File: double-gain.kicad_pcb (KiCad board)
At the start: 2 copper layers, 37.5 x 97.5 mm, 39 parts, among them J1 Conn_01x01_Female, J10 Conn_01x01_Female, J11 Conn_01x01_Female, J2 Conn_01x01_Female, J3 Conn_01x01_Female, J4 Conn_01x01_Female, J6 Conn_01x01_Female, J7 Conn_01x01_Female, J8 Conn_01x01_Female, J9 Conn_01x01_Female, U1 NE5534, U2 NE5534

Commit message: Add files via upload
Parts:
- renumbered C7 to C5, C8 to C7, C10 to C8

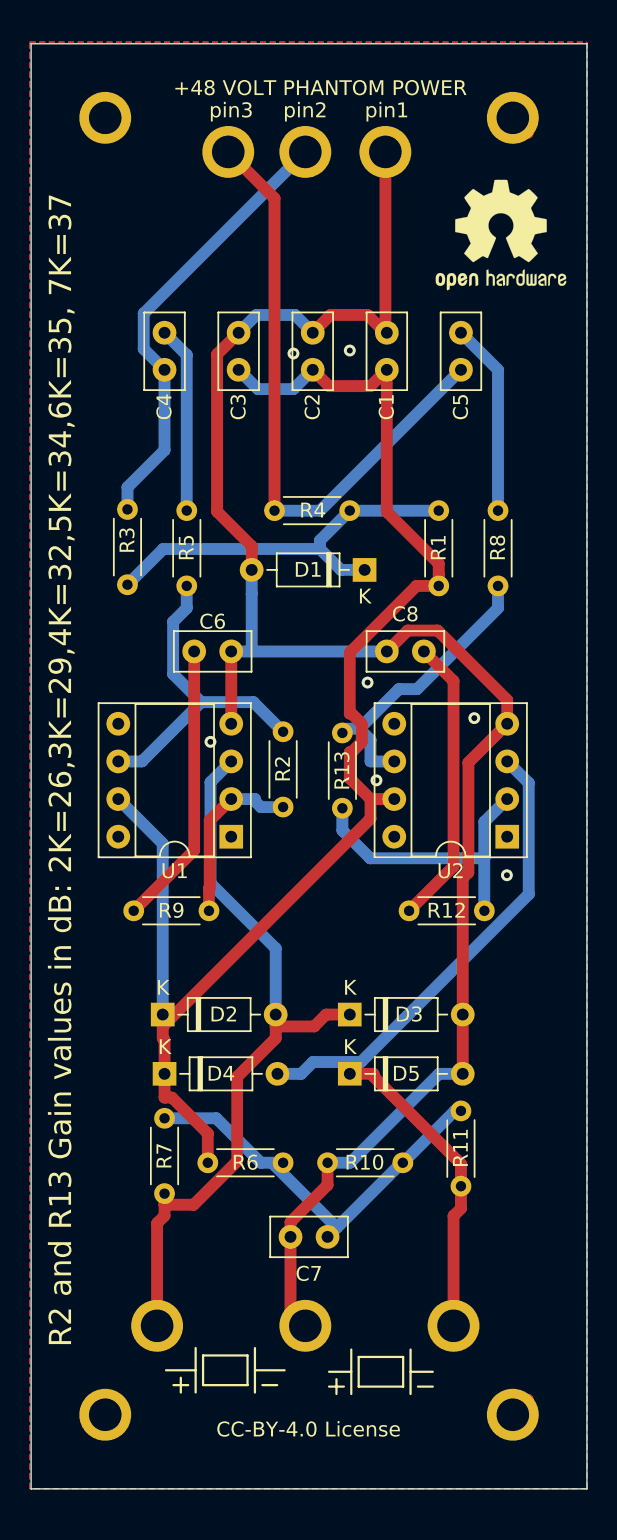
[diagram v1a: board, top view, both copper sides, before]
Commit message: Add files via upload
Replaced the opamp with a better one, with less power drain. Also added RF killer capacitor, C9 and C10.
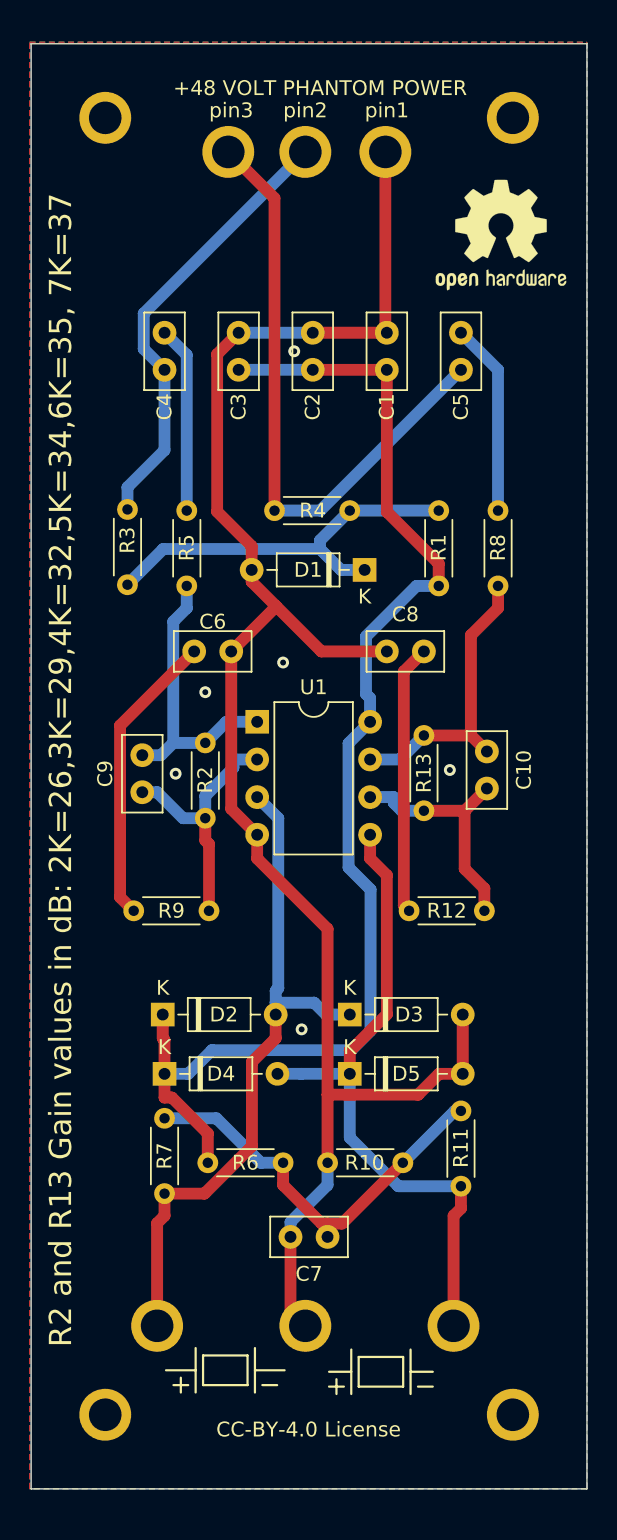
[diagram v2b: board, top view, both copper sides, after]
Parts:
- removed U2: NE5534, Package_DIP:DIP-8_W7.62mm_Socket
- added C10: 47uF, Capacitor_THT:C_Disc_D5.0mm_W2.5mm_P2.50mm, F.Cu at (68.2, 82.8)
- added C9: 47uF, Capacitor_THT:C_Disc_D5.0mm_W2.5mm_P2.50mm, F.Cu at (45.0, 83.0)
- D1: value 1N4746A (18V) -> HZ11B3-E
- U1: value NE5534 -> TL082; footprint Package_DIP:DIP-8_W7.62mm_Socket -> Package_DIP:DIP-8_W7.62mm
- moved U1 7.95 mm to (52.8, 78.2), turned to 0 degrees
- moved R13 5.50 mm to (64.0, 79.2)
- moved R2 5.30 mm to (49.2, 79.7)
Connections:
- R12 pad 2: Net-(R12-Pad2) -> Net-(C10-Pad1)
- R13 pad 1: Net-(R13-Pad1) -> Net-(C10-Pad2)
- R13 pad 2: Net-(R12-Pad2) -> Net-(C10-Pad1)
- R2 pad 1: Net-(R2-Pad1) -> Net-(C9-Pad2)
- R5 pad 2: Net-(R2-Pad1) -> Net-(C9-Pad2)
- R8 pad 2: Net-(R13-Pad1) -> Net-(C10-Pad2)
- U1 pad 1: Net-(U1-Pad1) -> Net-(C9-Pad2)
- U1 pad 5: Net-(U1-Pad5) -> ind
- U1 pad 6: Net-(R2-Pad1) -> Net-(C10-Pad1)
- U1 pad 7: VCC -> Net-(C10-Pad2)
- U1 pad 8: Net-(U1-Pad8) -> VCC
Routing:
- net Net-(R2-Pad1): track 22.6 -> 0.00 mm
- net Net-(R12-Pad2): track 20.0 -> 0.00 mm
- net Net-(C10-Pad2): track 0.00 -> 19.8 mm
- net Net-(C9-Pad2): track 0.00 -> 19.6 mm
- net Net-(R13-Pad1): track 19.6 -> 0.00 mm
- net Net-(C10-Pad1): track 0.00 -> 16.4 mm
- net VCC: track 97.2 -> 86.9 mm
- net ind: track 53.6 -> 45.4 mm
- net Net-(C9-Pad1): track 12.0 -> 17.7 mm
- net V-: track 123.8 -> 119.3 mm
- net Net-(D2-Pad2): track 51.0 -> 46.6 mm
- net Earth: track 3.04 -> 0.00 mm, vias 7 -> 6
- net Net-(C8-Pad2): track 19.6 -> 18.2 mm
- net Net-(C6-Pad2): track 19.2 -> 20.0 mm

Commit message: Add files via upload
fixed value of C9 and C10.
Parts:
- C10, C9: value 47uF -> 47pF
- U1: value TL082 -> TL082BCP

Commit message: Add files via upload
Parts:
- removed the C6 at (51.0, 73.5)
- removed the C8 at (61.5, 73.5)
- removed the J10 at (66.0, 119.0)
- removed J11: Conn_01x01_Female, MountingHole:MountingHole_2.2mm_M2_ISO7380_Pad
- removed REF**: OSHW-Logo2_9.8x8mm_SilkScreen, Symbol:OSHW-Logo2_9.8x8mm_SilkScreen
- added C10: 47uF, Capacitor_THT:CP_Radial_D8.0mm_P3.50mm, F.Cu at (68.5, 74.5)
- added C7: 47uF, Capacitor_THT:CP_Radial_D8.0mm_P3.50mm, F.Cu at (45.5, 74.5)
- added J5: Conn_01x01_Female, MountingHole:MountingHole_2.2mm_M2_ISO7380_Pad, F.Cu at (46.0, 118.8)
- added J6: Conn_01x01_Female, MountingHole:MountingHole_2.2mm_M2_ISO7380_Pad, F.Cu at (61.5, 40.0)
- moved J1 79.6 mm to (56.0, 40.0)
- moved J2 79.6 mm to (66.0, 118.8)
- moved J4 79.2 mm to (55.8, 118.8)
- moved J3 0.28 mm to (51.0, 40.0)
- moved C9 0.25 mm to (68.2, 83.0)
- moved R13 0.25 mm to (64.0, 79.4)
- moved U1 0.25 mm to (52.8, 78.0)
- renumbered C9 to C6, C7 to C8, C10 to C9, D4 to D2, D5 to D3, D2 to D4, D3 to D5, J9 to J10, J6 to J7, J7 to J8, J8 to J9, R2 to R11, R6 to R2, R11 to R3, R7 to R4, R3 to R5, R4 to R6, R5 to R7
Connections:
- D4 pad 2: Net-(D2-Pad2) -> Net-(D4-Pad2)
- D5 pad 1: Net-(D2-Pad2) -> Net-(D4-Pad2)
- J1 pad 1: Net-(D2-Pad2) -> /2
- J2 pad 1: /2 -> ind
- R4 pad 2: Net-(D2-Pad2) -> Net-(D4-Pad2)
- U1 pad 3: Net-(D2-Pad2) -> Net-(D4-Pad2)
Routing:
- net Net-(D4-Pad2): track 0.00 -> 46.6 mm
- net Net-(D2-Pad2): track 46.6 -> 0.00 mm
- net V-: track 119.3 -> 125.6 mm
- net Net-(C7-Pad1): track 20.0 -> 17.7 mm
- net Net-(C10-Pad1): track 18.2 -> 20.2 mm
